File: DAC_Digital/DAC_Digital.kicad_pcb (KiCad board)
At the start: 2 copper layers, 100 x 100 mm, 131 parts, among them J1 +5V_in, J10 USB_Dev4, J11 P9, J12 Anlg_in, J13 Anlg_I2C, J14 P8, J15 Test, J16 Test, J17 Fix, J18 Fix, J19 Fix, J2 DBG_PORT, J20 Fix, J3 DSPL_PORT, J4 Out_SPDIF, J5 USB0, J6 USB1, J7 USB_Dev1, J8 USB_Dev2, J9 USB_Dev3, Q1 2n7002, Q2 2N7002, Q3 FDS4435, Q4 FDS4435, Q5 2N7002, Q6 2N7002, T1 DA103C, U1 CS8406_2, U2 PIC18F6722, U3 74LVC1G08GW, U4 PCM2903C, U5 74LVC1G08GW, U6 USB2514B-AEZC, U7 NE5532, X1 7A-24.000MAAJ-T, Y1 10MHz, Y2 12MHz

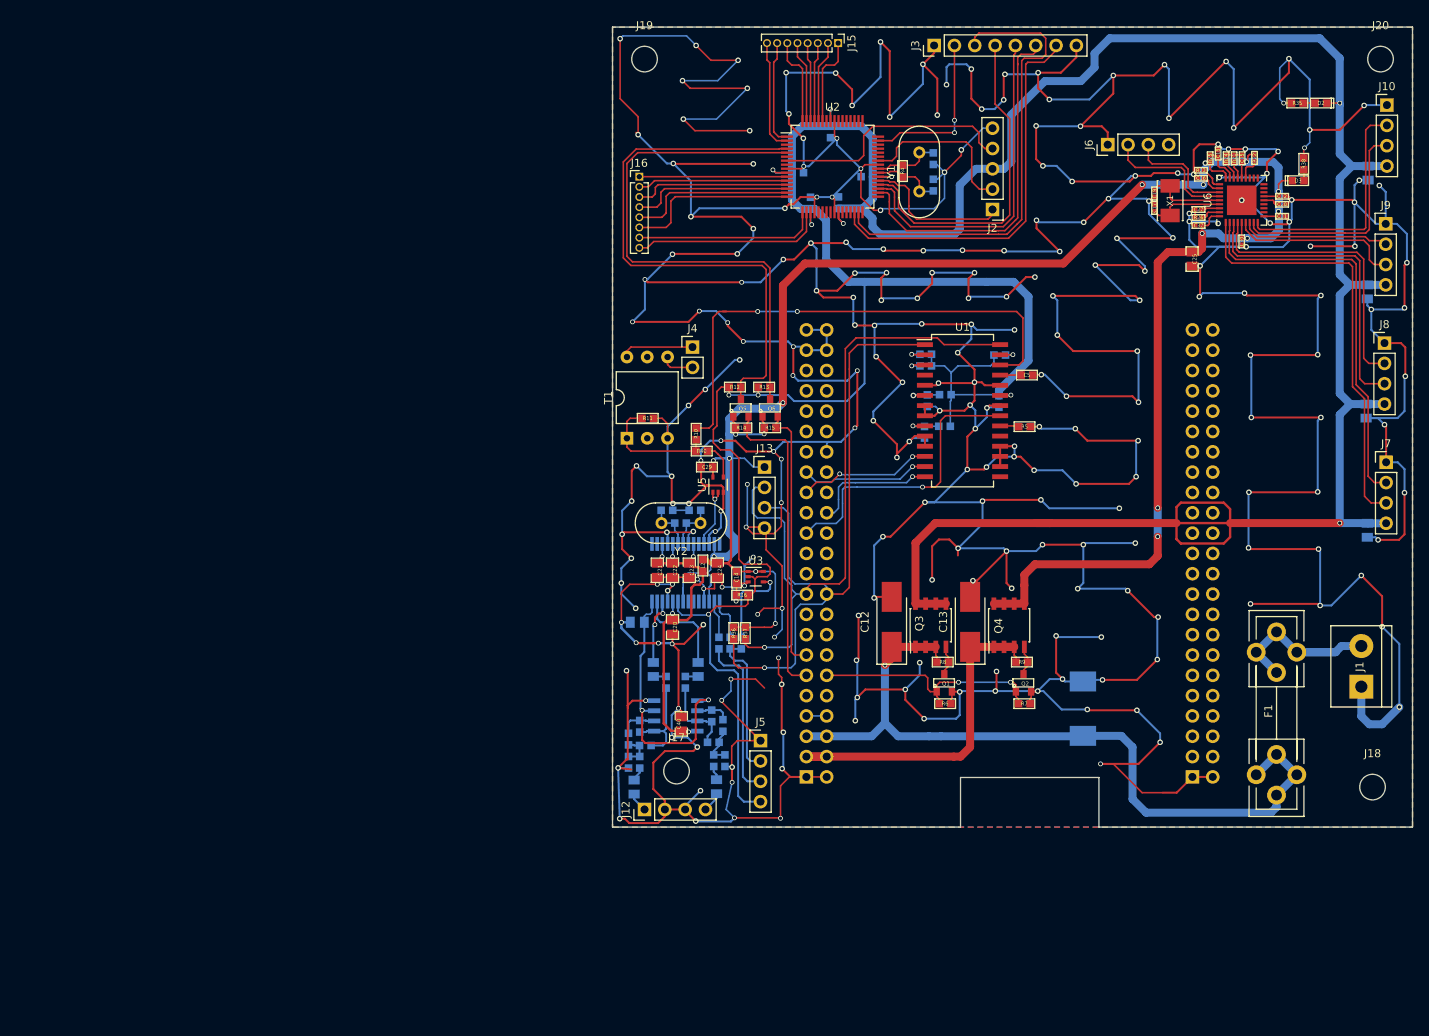
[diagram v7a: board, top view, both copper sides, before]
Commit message: Send Gerber DAC_Analog and DAC_Digital
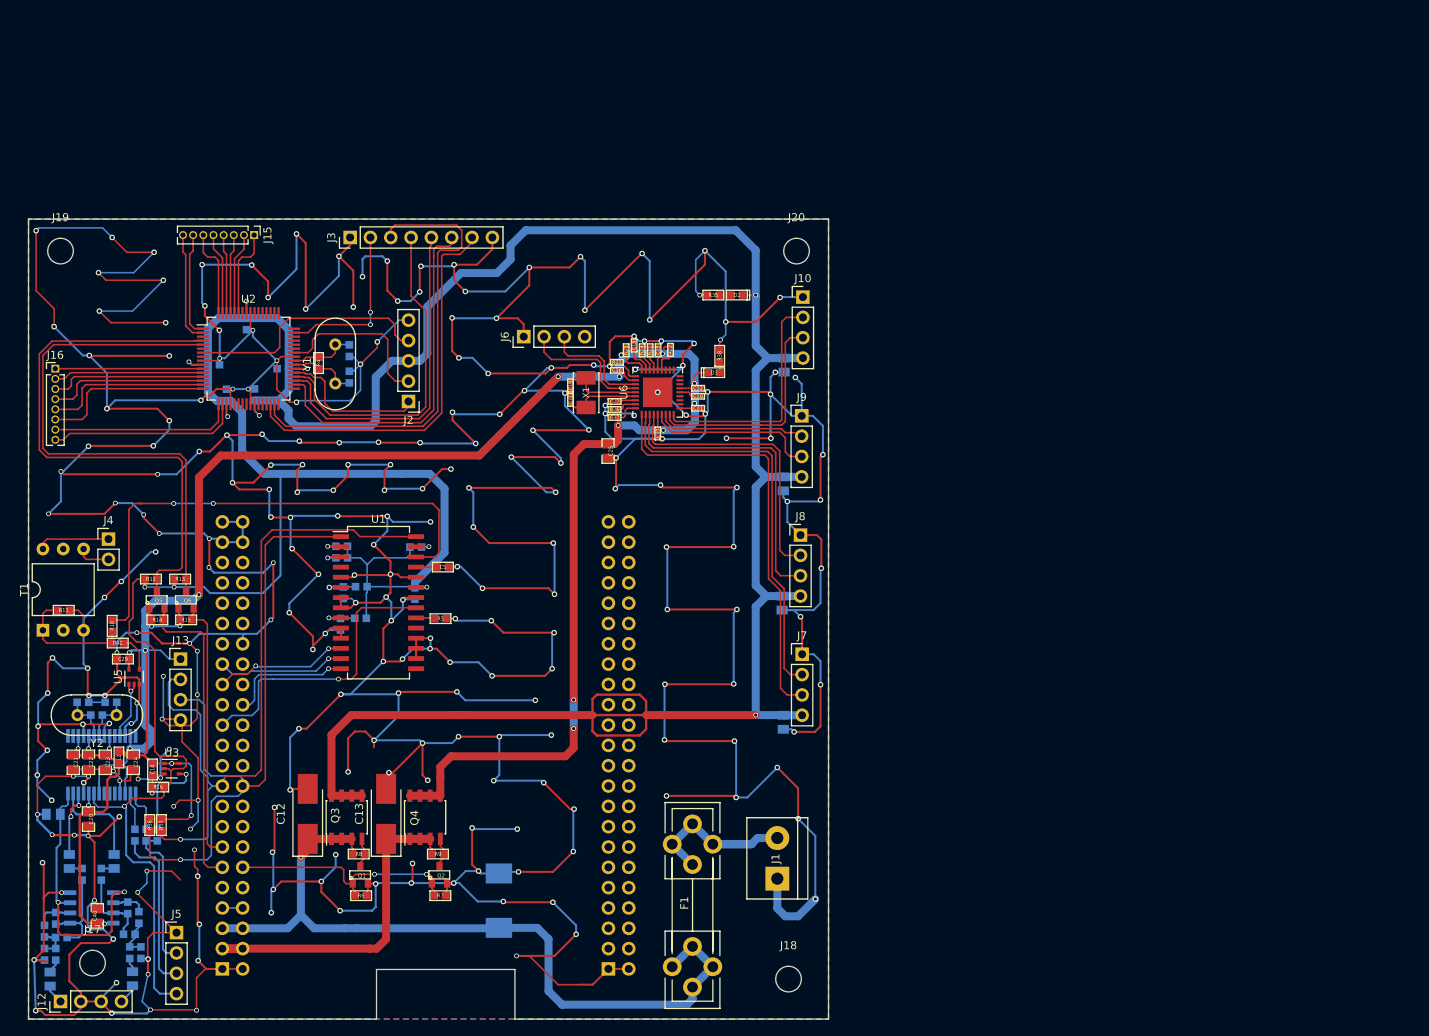
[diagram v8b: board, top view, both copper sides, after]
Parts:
- moved C3 76.8 mm to (70.3, 134.8)
- moved C36 76.8 mm to (95.5, 106.9)
- moved C5 76.8 mm to (73.8, 131.5)
- moved D1 76.8 mm to (80.8, 173.2)
- moved D2 76.8 mm to (110.5, 97.5)
- moved J10 76.8 mm to (118.8, 97.8)
- moved J14 76.8 mm to (94.5, 181.7)
- moved R23 76.8 mm to (95.5, 105.9)
- moved R9 76.8 mm to (73.2, 167.4)
- moved C1 76.8 mm to (61.0, 138.7)
- moved C10 76.8 mm to (53.8, 106.7)
- moved C11 76.8 mm to (49.2, 101.1)
- moved C12 76.8 mm to (56.9, 162.3)
- moved C14 76.8 mm to (37.5, 156.8)
- moved C15 76.8 mm to (32.3, 148.4)
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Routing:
- net Net-(J19-Pad1): vias 1 -> 0
